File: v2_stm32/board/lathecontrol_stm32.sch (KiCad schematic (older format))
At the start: 27 parts, among them J1 Conn_01x06_Male, J3 Barrel_Jack_Switch, J4 USB_B_Micro, J5 Conn_01x05_Male, J6 Conn_01x05_Male, J7 Conn_01x14_Female, J8 Conn_01x24, U1 STM32F103RBTx, Y1 8MHz

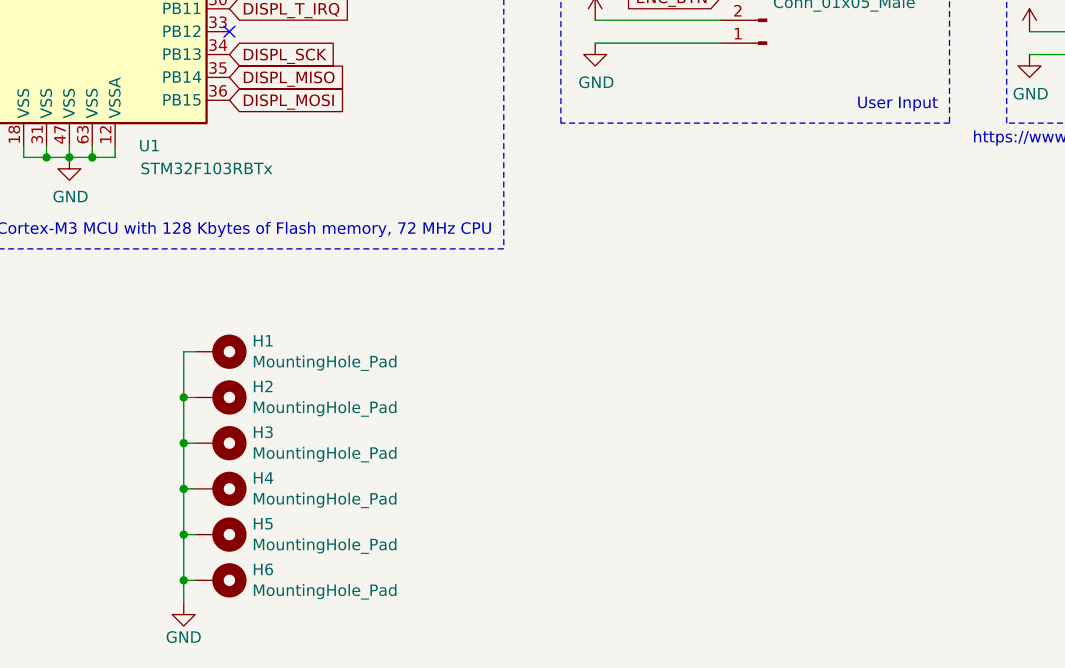
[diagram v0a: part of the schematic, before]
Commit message: Moved to 4 layer PCB. More routing
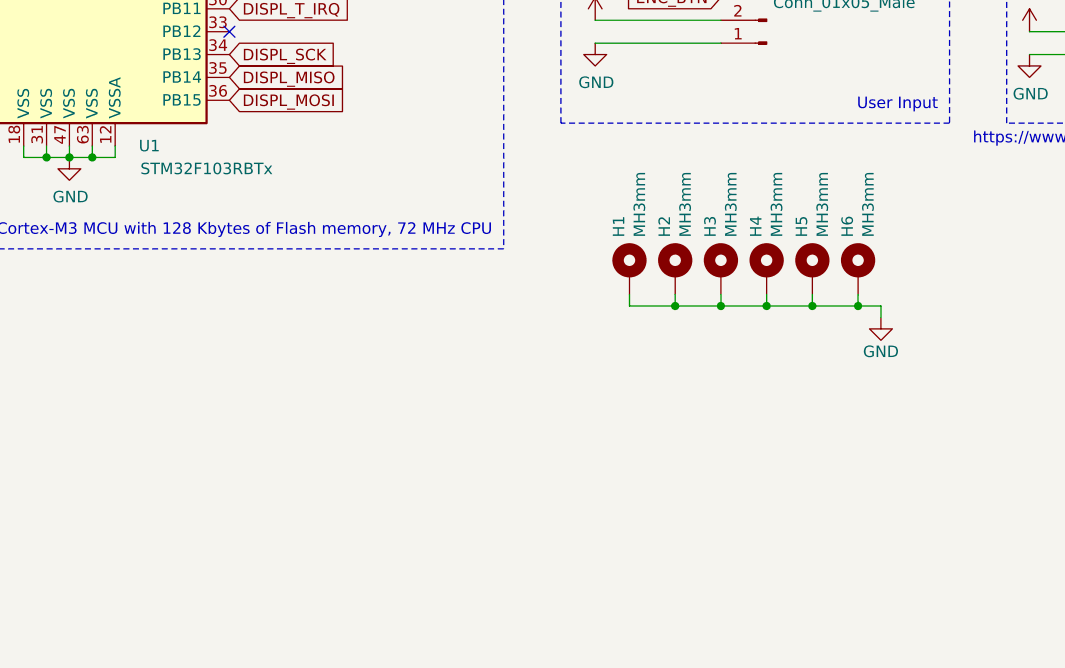
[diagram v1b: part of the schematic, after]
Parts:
- H1, H2, H3, H4, H5, H6: value MountingHole_Pad -> MH3mm
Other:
- moved on the sheet: H1, H2, H3, H4, H5, H6
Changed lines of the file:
@@
 	1    0    0    -1
 $EndComp
-$Comp
-L Mechanical:MountingHole_Pad H1
-U 1 1 607457E0
-P 5450 6400
-F 0 "H1" V 5404 6550 50  0000 L CNN
-F 1 "MountingHole_Pad" V 5495 6550 50  0000 L CNN
-F 2 "MountingHole:MountingHole_3mm_Pad" H 5450 6400 50  0001 C CNN
-F 3 "~" H 5450 6400 50  0001 C CNN
-	1    5450 6400
-	0    1    1    0
-$EndComp
 Wire Wire Line
-	5350 6400 5300 6400
+	7250 6150 7250 6200
 Wire Wire Line
-	5300 6400 5300 6600
+	7250 6200 7450 6200
 Wire Wire Line
-	5300 7000 5350 7000
+	7850 6200 7850 6150
 Wire Wire Line
-	5350 6800 5300 6800
-Connection ~ 5300 6800
+	7650 6150 7650 6200
+Connection ~ 7650 6200
 Wire Wire Line
-	5300 6800 5300 7000
+	7650 6200 7850 6200
 Wire Wire Line
-	5350 6600 5300 6600
-Connection ~ 5300 6600
+	7450 6150 7450 6200
+Connection ~ 7450 6200
 Wire Wire Line
-	5300 6600 5300 6800
+	7450 6200 7650 6200
 $Comp
 L power:GND #PWR022
 U 1 1 607536DA
-P 5300 7500
-F 0 "#PWR022" H 5300 7250 50  0001 C CNN
-F 1 "GND" H 5300 7350 50  0000 C CNN
-F 2 "" H 5300 7500 50  0001 C CNN
-F 3 "" H 5300 7500 50  0001 C CNN
-	1    5300 7500
+P 8350 6250
+F 0 "#PWR022" H 8350 6000 50  0001 C CNN
+F 1 "GND" H 8350 6100 50  0000 C CNN
+F 2 "" H 8350 6250 50  0001 C CNN
+F 3 "" H 8350 6250 50  0001 C CNN
+	1    8350 6250
 	1    0    0    -1
 $EndComp
-Connection ~ 5300 7000
-$Comp
-L Mechanical:MountingHole_Pad H2
-U 1 1 60758670
-P 5450 6600
-F 0 "H2" V 5404 6750 50  0000 L CNN
-F 1 "MountingHole_Pad" V 5495 6750 50  0000 L CNN
-F 2 "MountingHole:MountingHole_3mm_Pad" H 5450 6600 50  0001 C CNN
-F 3 "~" H 5450 6600 50  0001 C CNN
-	1    5450 6600
-	0    1    1    0
-$EndComp
-$Comp
-L Mechanical:MountingHole_Pad H3
-U 1 1 607589EB
-P 5450 6800
-F 0 "H3" V 5404 6950 50  0000 L CNN
-F 1 "MountingHole_Pad" V 5495 6950 50  0000 L CNN
-F 2 "MountingHole:MountingHole_3mm_Pad" H 5450 6800 50  0001 C CNN
-F 3 "~" H 5450 6800 50  0001 C CNN
-	1    5450 6800
-	0    1    1    0
-$EndComp
-$Comp
-L Mechanical:MountingHole_Pad H4
-U 1 1 60758C90
-P 5450 7000
-F 0 "H4" V 5404 7150 50  0000 L CNN
-F 1 "MountingHole_Pad" V 5495 7150 50  0000 L CNN
-F 2 "MountingHole:MountingHole_3mm_Pad" H 5450 7000 50  0001 C CNN
-F 3 "~" H 5450 7000 50  0001 C CNN
-	1    5450 7000
-	0    1    1    0
-$EndComp
-$Comp
-L Mechanical:MountingHole_Pad H5
-U 1 1 607AC43A
-P 5450 7200
-F 0 "H5" V 5404 7350 50  0000 L CNN
-F 1 "MountingHole_Pad" V 5495 7350 50  0000 L CNN
-F 2 "MountingHole:MountingHole_3mm_Pad" H 5450 7200 50  0001 C CNN
-F 3 "~" H 5450 7200 50  0001 C CNN
-	1    5450 7200
-	0    1    1    0
-$EndComp
-$Comp
-L Mechanical:MountingHole_Pad H6
-U 1 1 607AC779
-P 5450 7400
-F 0 "H6" V 5404 7550 50  0000 L CNN
-F 1 "MountingHole_Pad" V 5495 7550 50  0000 L CNN
-F 2 "MountingHole:MountingHole_3mm_Pad" H 5450 7400 50  0001 C CNN
-F 3 "~" H 5450 7400 50  0001 C CNN
-	1    5450 7400
-	0    1    1    0
-$EndComp
+Connection ~ 7850 6200
 Wire Wire Line
-	5300 7200 5350 7200
+	8050 6200 8050 6150
 Wire Wire Line
-	5300 7000 5300 7200
+	7850 6200 8050 6200
 Wire Wire Line
-	5300 7200 5300 7400
+	8050 6200 8250 6200
 Wire Wire Line
-	5300 7400 5350 7400
-Connection ~ 5300 7200
+	8250 6200 8250 6150
+Connection ~ 8050 6200
 Wire Wire Line
-	5300 7400 5300 7500
-Connection ~ 5300 7400
+	8250 6200 8350 6200
+Connection ~ 8250 6200
 $Comp
 L power:+3.3V #PWR0102
@@
 NoConn ~ 5500 2100
 $Comp
-L power:GND #PWR?
+L power:GND #PWR051
 U 1 1 608AE751
 P 6350 2550
-F 0 "#PWR?" H 6350 2300 50  0001 C CNN
+F 0 "#PWR051" H 6350 2300 50  0001 C CNN
 F 1 "GND" H 6355 2377 50  0000 C CNN
 F 2 "" H 6350 2550 50  0001 C CNN
@@
 Wire Wire Line
 	6350 2200 6350 2250
+$Comp
+L Mechanical:MountingHole_Pad H6
+U 1 1 607AC779
+P 8250 6050
+F 0 "H6" V 8204 6200 50  0000 L CNN
+F 1 "MH3mm" V 8295 6200 50  0000 L CNN
+F 2 "MountingHole:MountingHole_3mm_Pad" H 8250 6050 50  0001 C CNN
+F 3 "~" H 8250 6050 50  0001 C CNN
+	1    8250 6050
+	1    0    0    -1
+$EndComp
+$Comp
+L Mechanical:MountingHole_Pad H5
+U 1 1 607AC43A
+P 8050 6050
+F 0 "H5" V 8004 6200 50  0000 L CNN
+F 1 "MH3mm" V 8095 6200 50  0000 L CNN
+F 2 "MountingHole:MountingHole_3mm_Pad" H 8050 6050 50  0001 C CNN
+F 3 "~" H 8050 6050 50  0001 C CNN
+	1    8050 6050
+	1    0    0    -1
+$EndComp
+$Comp
+L Mechanical:MountingHole_Pad H4
+U 1 1 60758C90
+P 7850 6050
+F 0 "H4" V 7804 6200 50  0000 L CNN
+F 1 "MH3mm" V 7895 6200 50  0000 L CNN
+F 2 "MountingHole:MountingHole_3mm_Pad" H 7850 6050 50  0001 C CNN
+F 3 "~" H 7850 6050 50  0001 C CNN
+	1    7850 6050
+	1    0    0    -1
+$EndComp
+$Comp
+L Mechanical:MountingHole_Pad H3
+U 1 1 607589EB
+P 7650 6050
+F 0 "H3" V 7604 6200 50  0000 L CNN
+F 1 "MH3mm" V 7695 6200 50  0000 L CNN
+F 2 "MountingHole:MountingHole_3mm_Pad" H 7650 6050 50  0001 C CNN
+F 3 "~" H 7650 6050 50  0001 C CNN
+	1    7650 6050
+	1    0    0    -1
+$EndComp
+$Comp
+L Mechanical:MountingHole_Pad H2
+U 1 1 60758670
+P 7450 6050
+F 0 "H2" V 7404 6200 50  0000 L CNN
+F 1 "MH3mm" V 7495 6200 50  0000 L CNN
+F 2 "MountingHole:MountingHole_3mm_Pad" H 7450 6050 50  0001 C CNN
+F 3 "~" H 7450 6050 50  0001 C CNN
+	1    7450 6050
+	1    0    0    -1
+$EndComp
+$Comp
+L Mechanical:MountingHole_Pad H1
+U 1 1 607457E0
+P 7250 6050
+F 0 "H1" V 7204 6200 50  0000 L CNN
+F 1 "MH3mm" V 7295 6200 50  0000 L CNN
+F 2 "MountingHole:MountingHole_3mm_Pad" H 7250 6050 50  0001 C CNN
+F 3 "~" H 7250 6050 50  0001 C CNN
+	1    7250 6050
+	1    0    0    -1
+$EndComp
+Wire Wire Line
+	8350 6200 8350 6250
 $EndSCHEMATC

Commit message: Started current loop output for frequency converter
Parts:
- removed C7: 100n, Capacitor_SMD:C_0603_1608Metric, symbol Device:C
- added C12: 10u, Capacitor_SMD:C_0805_2012Metric, symbol Device:C
- renumbered C6 to C7
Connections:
- net +5V: now also C12.1
- net GND: now also C12.2
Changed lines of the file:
@@
 $Descr A4 11693 8268
 encoding utf-8
-Sheet 1 7
+Sheet 1 8
 Title ""
 Date ""
@@
 AR Path="/60265FC9/6029BFB8" Ref="C?"  Part="1"
 AR Path="/6026601C/6029BFB8" Ref="C?"  Part="1"
-AR Path="/6029BFB8" Ref="C6"  Part="1"
-F 0 "C6" H 4615 1246 50  0000 L CNN
+AR Path="/6029BFB8" Ref="C7"  Part="1"
+F 0 "C7" H 4615 1246 50  0000 L CNN
 F 1 "100n" H 4615 1155 50  0000 L CNN
 F 2 "Capacitor_SMD:C_0603_1608Metric" H 4538 1050 50  0001 C CNN
@@
 F 4 "C14663" H 4500 1200 50  0001 C CNN "LCSC"
 	1    4500 1200
-	1    0    0    -1
-$EndComp
-$Comp
-L Device:C C?
-U 1 1 6029C42F
-P 4950 1200
-AR Path="/6025D9E2/6029C42F" Ref="C?"  Part="1"
-AR Path="/6025D9E2/6025E7C0/6029C42F" Ref="C?"  Part="1"
-AR Path="/6025D9E2/60265A76/6029C42F" Ref="C?"  Part="1"
-AR Path="/6025D9E2/60265B58/6029C42F" Ref="C?"  Part="1"
-AR Path="/6025D9E2/60265BB4/6029C42F" Ref="C?"  Part="1"
-AR Path="/6025D9E2/60265C25/6029C42F" Ref="C?"  Part="1"
-AR Path="/60265C89/6029C42F" Ref="C?"  Part="1"
-AR Path="/60265F6D/6029C42F" Ref="C?"  Part="1"
-AR Path="/60265FC9/6029C42F" Ref="C?"  Part="1"
-AR Path="/6026601C/6029C42F" Ref="C?"  Part="1"
-AR Path="/6029C42F" Ref="C7"  Part="1"
-F 0 "C7" H 5065 1246 50  0000 L CNN
-F 1 "100n" H 5065 1155 50  0000 L CNN
-F 2 "Capacitor_SMD:C_0603_1608Metric" H 4988 1050 50  0001 C CNN
-F 3 "https://datasheet.lcsc.com/szlcsc/YAGEO-CC0603KRX7R9BB104_C14663.pdf" H 4950 1200 50  0001 C CNN
-F 4 "C14663" H 4950 1200 50  0001 C CNN "LCSC"
-	1    4950 1200
 	1    0    0    -1
 $EndComp
@@
 	3150 1400 3600 1400
 Wire Wire Line
-	4950 1400 4950 1350
-Wire Wire Line
 	3600 1350 3600 1400
 Connection ~ 3600 1400
@@
 Wire Wire Line
 	4500 1350 4500 1400
-Connection ~ 4500 1400
-Wire Wire Line
-	4500 1400 4950 1400
 Wire Wire Line
 	3150 1050 3150 1000
@@
 	3150 1000 3600 1000
 Wire Wire Line
-	4950 1000 4950 1050
-Wire Wire Line
 	4500 1050 4500 1000
-Connection ~ 4500 1000
-Wire Wire Line
-	4500 1000 4950 1000
 Wire Wire Line
 	3600 1050 3600 1000
@@
 Wire Wire Line
 	8350 6200 8350 6250
+$Comp
+L power:GND #PWR?
+U 1 1 605079AF
+P 10300 4300
+AR Path="/60278C87/605079AF" Ref="#PWR?"  Part="1"
+AR Path="/605079AF" Ref="#PWR015"  Part="1"
+F 0 "#PWR015" H 10300 4050 50  0001 C CNN
+F 1 "GND" H 10305 4127 50  0000 C CNN
+F 2 "" H 10300 4300 50  0001 C CNN
+F 3 "" H 10300 4300 50  0001 C CNN
+	1    10300 4300
+	1    0    0    -1
+$EndComp
+$Comp
+L Device:C C?
+U 1 1 605079B6
+P 10300 4150
+AR Path="/6025D9E2/605079B6" Ref="C?"  Part="1"
+AR Path="/6025D9E2/6025E7C0/605079B6" Ref="C?"  Part="1"
+AR Path="/6025D9E2/60265A76/605079B6" Ref="C?"  Part="1"
+AR Path="/6025D9E2/60265B58/605079B6" Ref="C?"  Part="1"
+AR Path="/6025D9E2/60265BB4/605079B6" Ref="C?"  Part="1"
+AR Path="/6025D9E2/60265C25/605079B6" Ref="C?"  Part="1"
+AR Path="/60265C89/605079B6" Ref="C?"  Part="1"
+AR Path="/60265F6D/605079B6" Ref="C?"  Part="1"
+AR Path="/60265FC9/605079B6" Ref="C?"  Part="1"
+AR Path="/6026601C/605079B6" Ref="C?"  Part="1"
+AR Path="/605079B6" Ref="C12"  Part="1"
+AR Path="/60278C87/605079B6" Ref="C?"  Part="1"
+F 0 "C12" H 10415 4196 50  0000 L CNN
+F 1 "10u" H 10415 4105 50  0000 L CNN
+F 2 "Capacitor_SMD:C_0805_2012Metric" H 10338 4000 50  0001 C CNN
+F 3 "https://datasheet.lcsc.com/szlcsc/Samsung-Electro-Mechanics-CL31A106KBHNNNE_C13585.pdf" H 10300 4150 50  0001 C CNN
+F 4 "C13585" H 10300 4150 50  0001 C CNN "LCSC"
+	1    10300 4150
+	1    0    0    -1
+$EndComp
+$Comp
+L power:+5V #PWR013
+U 1 1 6050A8C0
+P 10300 4000
+F 0 "#PWR013" H 10300 3850 50  0001 C CNN
+F 1 "+5V" H 10315 4173 50  0000 C CNN
+F 2 "" H 10300 4000 50  0001 C CNN
+F 3 "" H 10300 4000 50  0001 C CNN
+	1    10300 4000
+	1    0    0    -1
+$EndComp
+$Sheet
+S 750  6750 1150 700
+U 60592617
+F0 "Current Loop Output" 50
+F1 "currentloop_output.sch" 50
+$EndSheet
 $EndSCHEMATC
